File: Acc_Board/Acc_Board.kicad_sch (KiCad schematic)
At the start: 49 parts, among them J1 AIRs Power, J12 776087-1, J3 IMD BAT, J4 HV Power, J5 HVIL, J6 IMD, J7 Current Sensor, J9 Shutdown IL, K1 Relay_SPST-NO, Q1 STS6NF20V, Q2 STS6NF20V, U1 ISO1050DUB, U15 MCP6004, U2 NUCLEO-L432KC, U4 PQDE6W-Q110-S5-H-D, U5 R-78B5.0-2.0, U8 LM7809_TO220

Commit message: traces for acc board, WIP
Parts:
- added J8: Fans, 1FS_2_Global_Footprint_Library:MOLEX_1053091206, symbol 1FS_2_Global_Symbol_Library:1053091206
- added Q3: STS6NF20V, 1FS_2_Global_Footprint_Library:SO-8_STM, symbol 1_ACC_BOARD:STS6NF20V
- added R11: 120, Resistor_SMD:R_0805_2012Metric_Pad1.20x1.40mm_HandSolder, symbol Device:R
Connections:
- net +12V: now also J8.2, J8.4, J8.6
- net GND: now also Q3.1 (S), Q3.2 (S), Q3.3 (S)
- net at D3.2 (A): now also R11.1; no longer U2.CN3_12 (PA8)
- net CAN1_RD: now reaches U1.2 (RXD), U2.CN3_13 (PA11)
- net CAN1_TD: now reaches U1.3 (TXD), U2.CN3_5 (PA12)
- new net: R11.2, U2.CN3_12 (PA8)
- new net: J8.1, J8.3, J8.5, Q3.5 (D), Q3.6 (D), Q3.7 (D), Q3.8 (D)
- new net Fan_Control: Q3.4 (G)
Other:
- note added: "Fans"
- note added: "Status Light"
- note removed: "CAN Status Light"
- note removed: "Check if the micro can directly power an LED check for resistance things"
- moved on the sheet: D3

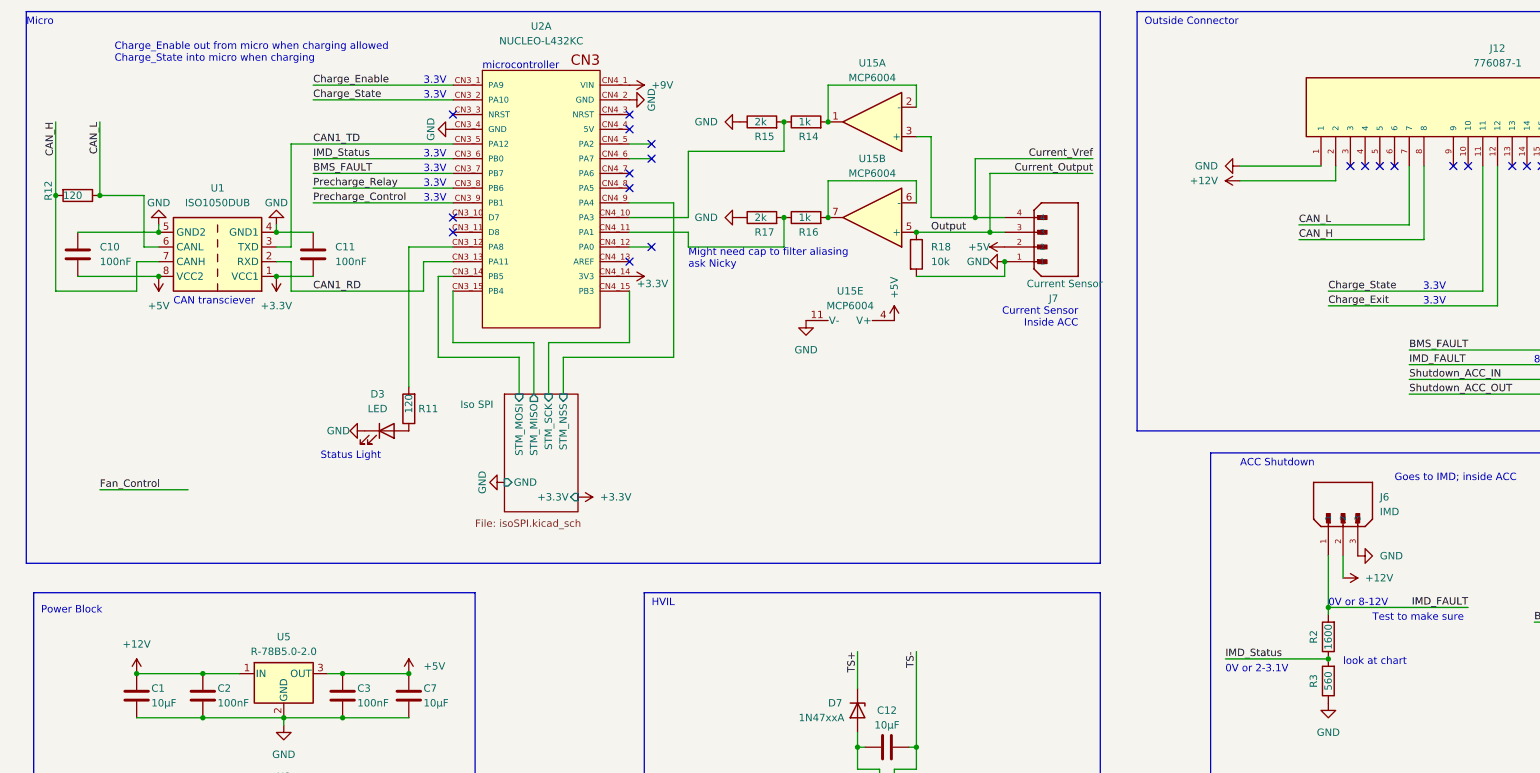
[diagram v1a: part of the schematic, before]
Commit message: more traces and fan control for acc board
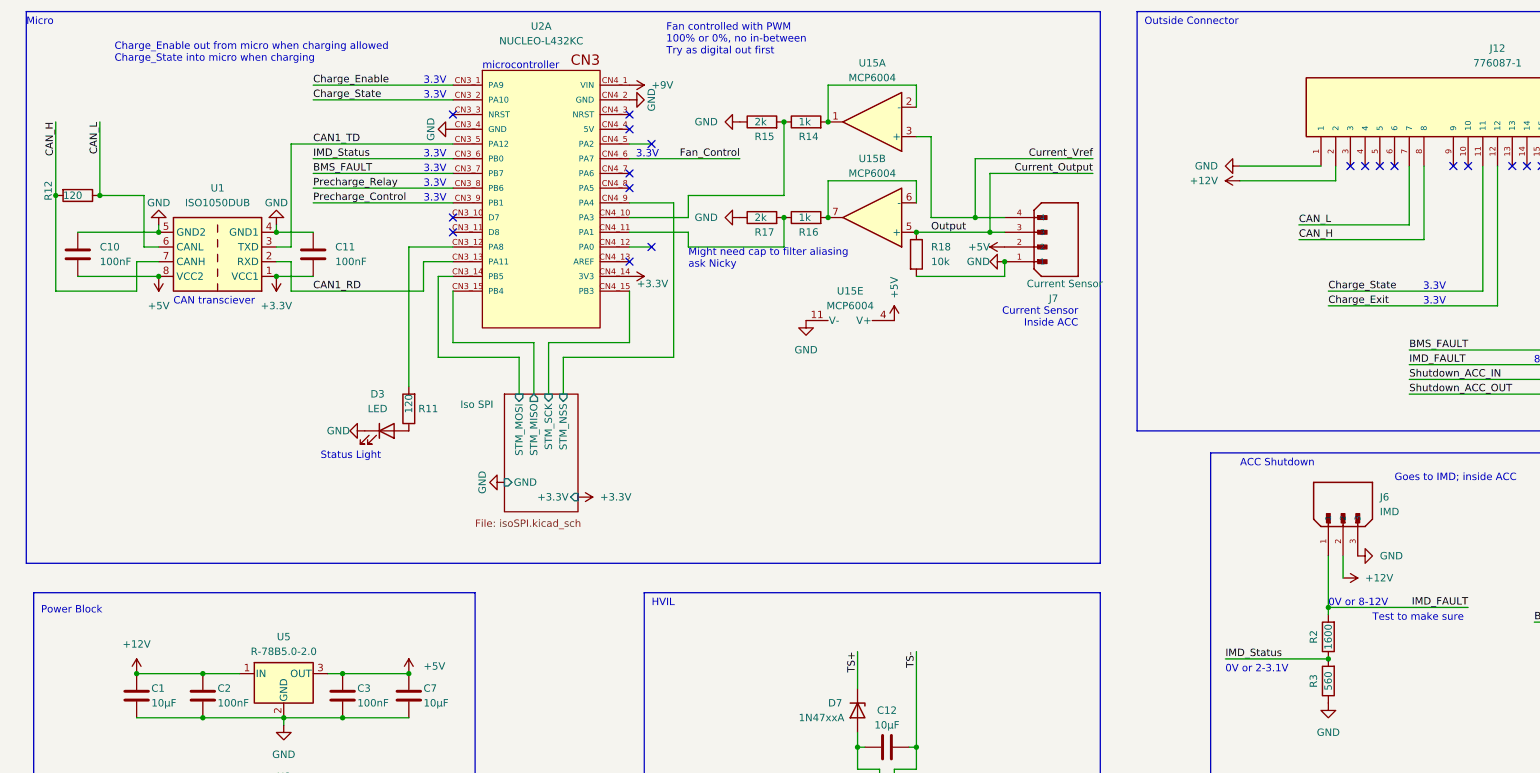
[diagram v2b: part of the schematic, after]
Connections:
- net Fan_Control: now also U2.CN4_6 (PA7)
- no-connect marks 27 -> 26
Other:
- note added: "Fan controlled with PWM 100% or 0%, no in-between Try as digital out first"
- note removed: "look at chart"
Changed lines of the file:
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@@
   (junction (at 73.66 217.17) (diameter 0) (color 0 0 0 0)
   )
-  (no_connect (at 127 43.18))
   (no_connect (at 172.72 189.23))
   (no_connect (at 307.34 41.91))
   (no_connect (at 96.52 53.34))
-  (no_connect (at 127 45.72))
   (no_connect (at 127 33.02))
   (no_connect (at 130.81 55.88))
@@
   (no_connect (at 373.38 151.13))
   (no_connect (at 96.52 33.02))
-  (no_connect (at 130.81 40.64))
+  (no_connect (at 127 45.72))
   (no_connect (at 130.81 38.1))
   (no_connect (at 254 41.91))
@@
   (no_connect (at 388.62 151.13))
   (no_connect (at 96.52 50.8))
+  (no_connect (at 127 43.18))
   (no_connect (at 256.54 41.91))
   (no_connect (at 269.24 41.91))
@@
     (stroke (width 0) (type default))
   )
-  (wire (pts (xy 137.16 39.37) (xy 137.16 50.8))
+  (wire (pts (xy 137.16 46.99) (xy 137.16 50.8))
     (stroke (width 0) (type default))
   )
@@
     (stroke (width 0) (type default))
   )
-  (wire (pts (xy 153.67 34.29) (xy 153.67 39.37))
+  (wire (pts (xy 153.67 34.29) (xy 153.67 46.99))
     (stroke (width 0) (type default))
   )
@@
     (stroke (width 0) (type default))
   )
-  (wire (pts (xy 35.56 97.79) (xy 50.8 97.79))
-    (stroke (width 0) (type default))
-  )
   (wire (pts (xy 76.2 217.17) (xy 76.2 203.2))
     (stroke (width 0) (type default))
@@
     (stroke (width 0) (type default))
   )
-  (wire (pts (xy 127 40.64) (xy 130.81 40.64))
-    (stroke (width 0) (type default))
-  )
   (wire (pts (xy 298.45 219.71) (xy 285.75 219.71))
     (stroke (width 0) (type default))
@@
     (stroke (width 0) (type default))
   )
-  (wire (pts (xy 153.67 39.37) (xy 137.16 39.37))
+  (wire (pts (xy 153.67 46.99) (xy 137.16 46.99))
     (stroke (width 0) (type default))
   )
   (wire (pts (xy 91.44 58.42) (xy 96.52 58.42))
+    (stroke (width 0) (type default))
+  )
+  (wire (pts (xy 127 40.64) (xy 146.05 40.64))
     (stroke (width 0) (type default))
   )
@@
     (effects (font (size 1.27 1.27)) (justify left bottom))
   )
+  (text "3.3V" (at 132.08 40.64 0)
+    (effects (font (size 1.27 1.27)) (justify right bottom))
+  )
   (text "3.3V" (at 91.44 27.94 0)
     (effects (font (size 1.27 1.27)) (justify left bottom))
@@
     (effects (font (size 1.27 1.27)) (justify left bottom))
   )
+  (text "Fan controlled with PWM\n100% or 0%, no in-between\nTry as digital out first"
+    (at 133.35 22.86 0)
+    (effects (font (size 1.27 1.27)) (justify left bottom))
+  )
   (text "+Vo" (at 170.18 179.07 90)
     (effects (font (size 1.27 1.27)) (justify left bottom))
@@
     (effects (font (size 1.27 1.27)) (justify left bottom))
   )
-  (text "look at chart" (at 250.19 128.27 0)
-    (effects (font (size 1.27 1.27)) (justify left bottom))
-  )
   (text "0V or 2-3.1V" (at 229.87 129.54 0)
     (effects (font (size 1.27 1.27)) (justify left bottom))
@@
     (effects (font (size 1.27 1.27)) (justify left bottom))
   )
-  (label "Fan_Control" (at 35.56 97.79 0) (fields_autoplaced)
-    (effects (font (size 1.27 1.27)) (justify left bottom))
-  )
   (label "Shutdown_ACC_OUT" (at 271.78 165.1 0) (fields_autoplaced)
     (effects (font (size 1.27 1.27)) (justify left bottom))
@@
     (effects (font (size 1.27 1.27)) (justify left bottom))
   )
+  (label "Fan_Control" (at 146.05 40.64 180) (fields_autoplaced)
+    (effects (font (size 1.27 1.27)) (justify right bottom))
+  )
   (label "Precharge_Relay" (at 40.64 227.33 180) (fields_autoplaced)

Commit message: Acc board traces done (for now)
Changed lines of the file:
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@@
     (fill (type none))
   )
-  (rectangle (start 24.13 115.57) (end 100.33 171.45)
+  (rectangle (start 24.13 115.57) (end 101.6 170.18)
     (stroke (width 0) (type default))
     (fill (type none))

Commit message: minor acc board changes
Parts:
- removed D4: US1A, Diode_SMD:D_SMA, symbol Diode:US1A
- removed U?: DK1A1B-12V, 1FS_2_Global_Footprint_Library:RELAY_DK2A_PAN, symbol 2FS-1_Symbol Library:DK1A1B-12V
- added C13, C15: C, Capacitor_SMD:C_0805_2012Metric_Pad1.18x1.45mm_HandSolder, symbol Device:C
- added J10: Conn_01x02_Pin, Connector_PinHeader_2.54mm:PinHeader_1x02_P2.54mm_Vertical, symbol Connector:Conn_01x02_Pin
- added R13: 3.9k, Resistor_SMD:R_0805_2012Metric_Pad1.20x1.40mm_HandSolder, symbol Device:R
- added R19: 18k, Resistor_SMD:R_0805_2012Metric_Pad1.20x1.40mm_HandSolder, symbol Device:R
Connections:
- net Charge_Exit is gone; now on net Charge_Enable: J12.12
- net +12V: now also R19.2
- net GND: now also C13.2, C15.1, J10.1 (Pin_1), R13.1
- net Buffered_C_Vref: now reaches R14.1, R15.2, U2.CN4_10 (PA3)
- net Buffered_C_Vref: now also C15.2
- net at U?.3: now also U?.4
- net Buffered_C_Out: now reaches R16.1, R17.2, U2.CN4_11 (PA1)
- net Buffered_C_Out: now also C13.1
- net GLV Voltage: now reaches U2.CN4_12 (PA0)
- net GLV Voltage: now also R13.2, R19.1
- net PA_2: now reaches U2.CN4_5 (PA2)
- net PA_2: now also J10.2 (Pin_2)
- no-connect marks 26 -> 24
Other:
- note added: "Status Light, Green"
- note removed: "Might need cap to filter aliasing ask Nicky"
- note removed: "Status Light"
- moved on the sheet: R14, R15, R16, R17, U15E

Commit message: added latching logic to acc board schematic
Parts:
- removed D1, D2, D5: US1A, Diode_SMD:D_SMA, symbol Diode:US1A
- added C17: 100nf, Capacitor_SMD:C_0805_2012Metric_Pad1.18x1.45mm_HandSolder, symbol Device:C
- added C4: 1uf, Capacitor_SMD:C_0805_2012Metric_Pad1.18x1.45mm_HandSolder, symbol Device:C
- added D1, D2, D4, D5 (x2): D, Diode_SMD:D_2010_5025Metric_Pad1.52x2.65mm_HandSolder, symbol Device:D
- added K2: Latching Relay, 1FS_2_Global_Footprint_Library:Omron G6BK-1114P-US, symbol 1_Personal_FS_Library:G6BK-1114P-US
- added Q4: STS6NF20V, 1FS_2_Global_Footprint_Library:SO-8_STM, symbol 1_ACC_BOARD:STS6NF20V
- added R20: 2.4M, Resistor_SMD:R_0805_2012Metric_Pad1.20x1.40mm_HandSolder, symbol Device:R
- added R21: 374, Resistor_SMD:R_0805_2012Metric_Pad1.20x1.40mm_HandSolder, symbol Device:R
- added R22: 665, Resistor_SMD:R_0805_2012Metric_Pad1.20x1.40mm_HandSolder, symbol Device:R
- added R23: 205, Resistor_SMD:R_0805_2012Metric_Pad1.20x1.40mm_HandSolder, symbol Device:R
- added U12: LM555N, Package_DIP:DIP-8_W7.62mm, symbol 2FS-1_Symbol Library:LM555N
- added U17: NAND, Package_DIP:DIP-14_W7.62mm, symbol 4xxx:4023
- added U? (x3): NSL-32, 1FS_2_Global_Footprint_Library:OptoCoupler 6-SOP, symbol Isolator:NSL-32
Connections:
- net +12V: now also D1.1 (K), U?.4 (R)
- net +5V: now also C17.2, C4.1, U12.4 (R), U12.8 (VCC), U17.14 (VDD), U?.4 (R), U?.4 (R)
- net BMS_FAULT: now also U?.1 (A); no longer U?.1 (A)
- net GND: now also C17.1, D2.2 (A), D5.2 (A), D5.2 (A), K2.1, Q4.1 (S), Q4.2 (S), Q4.3 (S), R20.2, R21.2, U12.1 (GND), U17.7 (VSS)
- net IMD_FAULT: now also U?.1 (A); no longer U?.1 (A)
- net Shutdown_ACC_OUT: now also K2.3; no longer J9.2
- net at K1.2, Q1.5 (D), Q1.6 (D)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: now also D1.2 (A)
- net at J9.1: now also K2.4; no longer U?.4
- net at U?.3 (R), U?.8 (+): now also D5.1 (K)
- net at U?.3 (R), U?.8 (+): now also D2.1 (K)
- new net: D4.2 (A), K2.2, Q4.5 (D), Q4.6 (D), Q4.7 (D), Q4.8 (D)
- new net: D4.1 (K), K2.5, U?.3 (R)
- new net: R22.1, U?.2 (K)
- new net: R23.1, U?.2 (K)
- new net: J9.2, U?.4
- new net: R21.1, U?.2 (K)
- new net: U17.9, U?.1 (A)
- new net: C4.2, R20.1, U12.2 (TR), U12.6 (THR)
- new net BMS_FAULT_5V: U17.8, U?.1 (A), U?.3 (R)
- new net IMD_FAULT_5V: U17.1, U17.2, U?.1 (A), U?.3 (R)
- new net IMD_Latch_Delay: Q4.4 (G), U12.3 (Q)
- new net SH_RESET: D5.1 (K), K2.6
- no-connect marks 24 -> 26
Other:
- note added: "The set part of the latch needs indep. power (fixed)"
- note added: "make cap smaller, resistor bigger (Done) 5V works!; connect to 5V DCDC"
- note added: "~3.5 sec 555 delay before turn on"
- moved on the sheet: J12, J6, J8, Q3, R10, R2, R3, R9, U?

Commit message: components placed on acc board; traces in progress
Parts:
- R21: value 374 -> 370
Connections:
- net BAT+: now also J4.3; no longer J4.2
- net BAT-: now also J4.4; no longer J4.1
- net BMS_FAULT: no longer J12.16
- net BMS_FAULT_5V: now also J12.16
- net GND: now also R22.2, R23.2
- net IMD_FAULT: no longer J12.17
- net IMD_FAULT_5V: now also J12.17
- net SH_RESET: now also J12.23
- net TS+: now also J4.1; no longer J4.4
- net TS-: now also J4.2; no longer J4.3
- net at K2.4: now also J9.2; no longer J9.1
- net at U?.4: now also J9.1; no longer J9.2
- no-connect marks 26 -> 25
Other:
- note removed: "8-12V"
- moved on the sheet: C17, C4, J8, J9, Q3, R20, R22, R23, U12, U17D, U?

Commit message: Acc board CAN fixes
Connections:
- net CAN_L_RES: now reaches J12.3
- net CAN_L_RES: now also R12.1
- net CAN_H_RES: now reaches J12.4
- net CAN_H_RES: now also R12.2
- net CAN_L_IN: now reaches J12.5
- net CAN_L_IN: now also J12.7, U1.6 (CANL)
- net CAN_H_IN: now reaches J12.6
- net CAN_H_IN: now also J12.8, U1.7 (CANH)
- removed net CAN_H: J12.8, R12.2, U1.7 (CANH)
- removed net CAN_L: J12.7, R12.1, U1.6 (CANL)
- no-connect marks 25 -> 21
